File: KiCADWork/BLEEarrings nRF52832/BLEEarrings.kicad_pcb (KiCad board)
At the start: 2 copper layers, 25.5 x 37.8 mm, 37 parts, among them J1 Screw_Terminal_01x01, J2 Screw_Terminal_01x02, J4 Conn_01x06_Pin, SW1 TK-6580B-1, U1 AP7343D-33W5-7, U2 nRF52832-QFxx, Y1 Crystal_GND23

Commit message: Small Bits
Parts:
- moved TP11 5.02 mm to (149.4, 73.6)
- moved J1 2.68 mm to (139.5, 72.4)
- moved J2 2.68 mm to (145.5, 72.4)
- moved C11 2.22 mm to (138.6, 50.5), turned to -90 degrees
- moved TP10 2.13 mm to (139.0, 68.1)
- moved C3 1.77 mm to (148.7, 49.9), turned to -90 degrees
- moved C4 1.71 mm to (144.3, 49.6), turned to 90 degrees
- moved C7 1.42 mm to (139.6, 50.5)
- moved TP3 1.26 mm to (139.5, 46.4)
- moved C6 0.75 mm to (140.5, 50.5), turned to -90 degrees
- moved Y1 0.75 mm to (146.5, 49.9)
- moved C5 0.69 mm to (147.8, 56.5), turned to 90 degrees
- moved L1 0.48 mm to (148.8, 56.5)
- moved TP4 0.42 mm to (149.3, 69.0)
- moved R9 0.33 mm to (149.4, 71.3)
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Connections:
- U1 pad 1: (no net) -> Net-(U1-EN)
- U1 pad 4: (no net) -> unconnected-(U1-NC-Pad4)
- U2 pad 42: unconnected-(U2-P0.30/AIN6-Pad42) -> Net-(U2-P0.30/AIN6)
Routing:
- net +3V3: track 5.12 -> 58.1 mm, vias 0 -> 2
- net NEO_LED: track 0.00 -> 20.3 mm, vias 0 -> 2
- net GND: track 26.3 -> 41.1 mm, vias 0 -> 24
- net +BATT: track 35.7 -> 48.8 mm
- net Net-(J2-Pin_1): track 0.00 -> 11.1 mm
- net Docked: track 0.00 -> 11.1 mm, vias 0 -> 2
- net Net-(U1-EN): track 0.00 -> 10.9 mm
- net LED_A: track 0.00 -> 8.96 mm, vias 0 -> 1
- net Net-(U2-DEC1): track 0.00 -> 2.25 mm
- net Net-(J4-Pin_2): track 9.24 -> 10.7 mm
- net Net-(U2-P0.30/AIN6): track 0.00 -> 0.98 mm, vias 0 -> 1
- net Net-(U2-XC2): track 4.60 -> 5.45 mm
- net Net-(U2-DEC4): track 2.15 -> 1.38 mm
- net Net-(U2-XC1): track 7.47 -> 8.00 mm
- net SWDIO: track 8.00 -> 8.50 mm
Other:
- board size 25.5 x 37.8 mm -> 25.5 x 35.8 mm

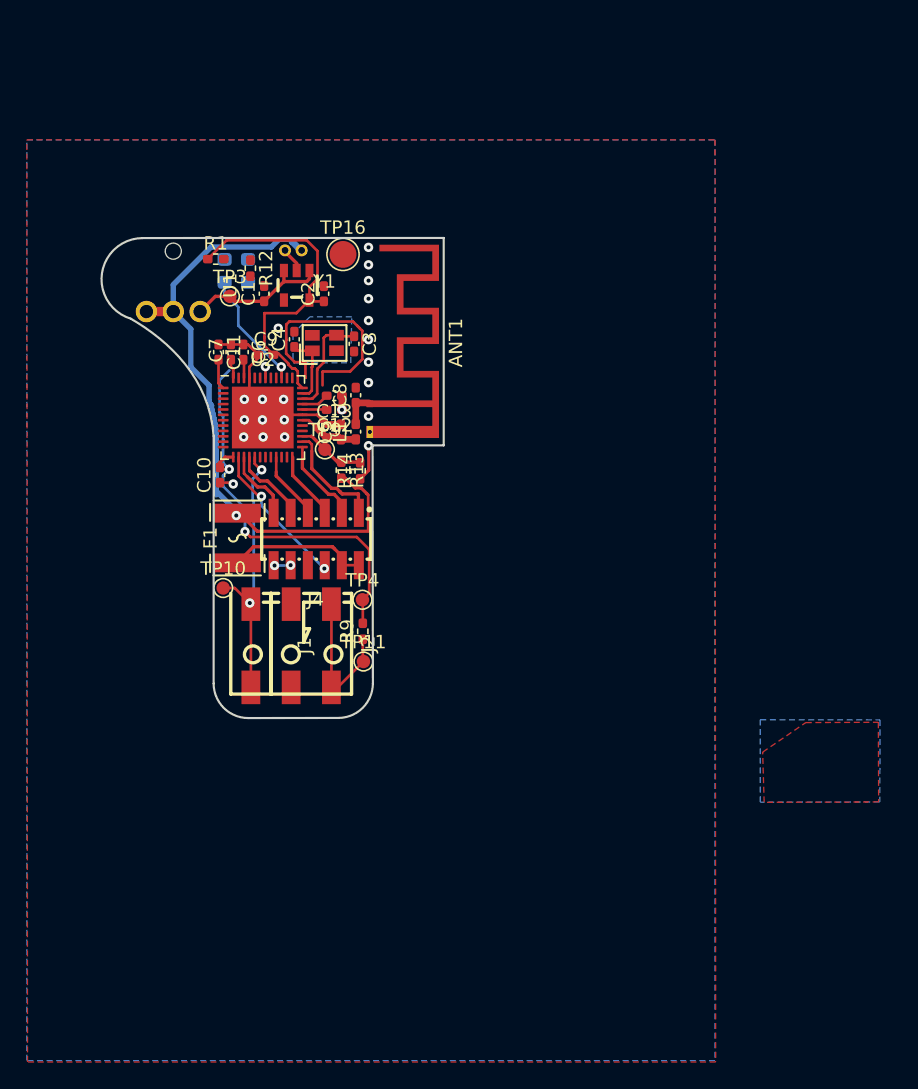
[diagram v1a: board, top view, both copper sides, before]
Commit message: New Chip NRF52833
large changes
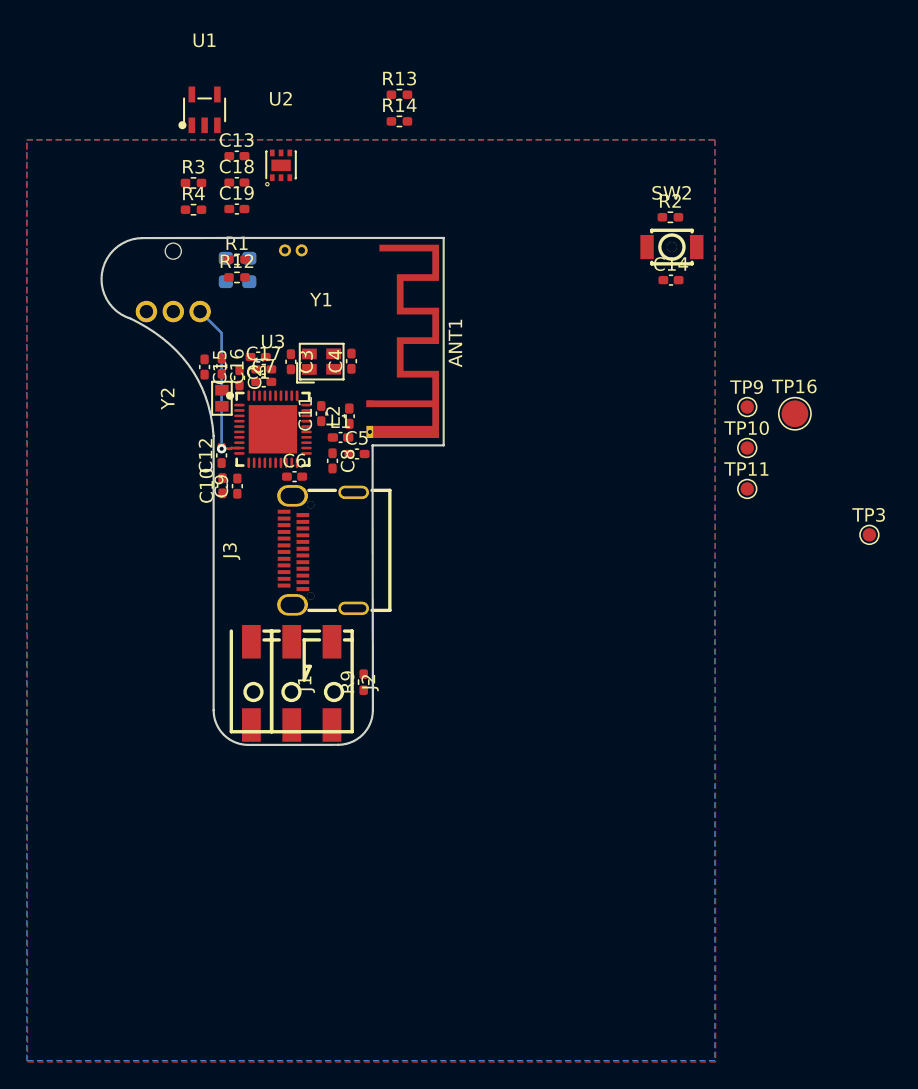
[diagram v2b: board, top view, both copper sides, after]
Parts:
- removed F1: BSMD1812-030-30V, easyeda2kicad:F1812
- removed J4: Conn_01x06_Pin, easyeda2kicad:HDR-SMD_PM127VS-12-12-H34-4.5-R
- removed TP4: TestPoint, TestPoint:TestPoint_Pad_D1.0mm
- added C14: 100n, Capacitor_SMD:C_0402_1005Metric_Pad0.74x0.62mm_HandSolder, F.Cu at (172.3, 45.2)
- added C15: 8p, Capacitor_SMD:C_0402_1005Metric_Pad0.74x0.62mm_HandSolder, F.Cu at (137.6, 51.7)
- added C16: 8p, Capacitor_SMD:C_0402_1005Metric_Pad0.74x0.62mm_HandSolder, F.Cu at (138.9, 51.6)
- added C17: NC, Capacitor_SMD:C_0402_1005Metric_Pad0.74x0.62mm_HandSolder, F.Cu at (142.0, 51.8)
- added C18: 100n, Capacitor_SMD:C_0402_1005Metric_Pad0.74x0.62mm_HandSolder, F.Cu at (140.0, 37.9)
- added C19: 10u, Capacitor_SMD:C_0402_1005Metric_Pad0.74x0.62mm_HandSolder, F.Cu at (140.0, 39.9)
- added J3: USB_C_Receptacle, easyeda2kicad:TYPE-C-SMD_C9900025773, F.Cu at (146.1, 65.3)
- added L2: 2.2n, Inductor_SMD:L_0402_1005Metric_Pad0.77x0.64mm_HandSolder, F.Cu at (148.4, 55.3)
- added R2: 2k, Resistor_SMD:R_0402_1005Metric_Pad0.72x0.64mm_HandSolder, F.Cu at (172.3, 40.5)
- added R3: 100, Resistor_SMD:R_0402_1005Metric_Pad0.72x0.64mm_HandSolder, F.Cu at (136.8, 38.0)
- added R4: 5k6, Resistor_SMD:R_0402_1005Metric_Pad0.72x0.64mm_HandSolder, F.Cu at (136.8, 39.9)
- added SW2: SW_DIP_x01, easyeda2kicad:KEY-SMD_L3.0-W2.5-LS4.0, F.Cu at (172.4, 42.7)
- added U3: NRF52833-QDAA-R7, easyeda2kicad:QFN-40_L5.0-W5.0-P0.40-TL-EP3.6, F.Cu at (142.7, 56.3)
- added Y2: Crystal, easyeda2kicad:CRYSTAL-SMD_L1.6-W1.0, F.Cu at (138.9, 54.0)
- C10, C9: value 100n -> 4.7u
- C11: value 100n -> 100p
- C12: value NC -> 4.7u
- C13: value 100p -> 10u
- C2, C6: value 1u -> 100n
- C3, C4: value 16p -> 12p
- C5: value 0.8p -> 1.2p
- C7: value 4.7u -> 1u
- C8: value 0.8p -> 1p
- D1: value RED LED -> WHITE LED
- L1: value 3.9n -> 4.7n
- R12: value 2k -> 220
- R13: value 5k1 -> 100k
- R14: value 5k1 -> 33k
- U1: value AP7343D-33W5-7 -> MCP73831T-2ACI/OT; footprint easyeda2kicad:SOT-23-5_L2.9-W1.6-P0.95-LS2.8-BR -> easyeda2kicad:SOT-23-5_L3.0-W1.7-P0.95-LS2.8-BL
- U2: value nRF52832-QFxx -> XB6096I2SV; footprint Package_DFN_QFN:QFN-48-1EP_6x6mm_P0.4mm_EP4.6x4.6mm -> easyeda2kicad:WDFN-6_L2.0-W2.0-P0.65-BL-EP
- moved TP3 50.8 mm to (187.1, 64.2)
- moved TP10 40.4 mm to (178.0, 57.7)
- moved TP16 35.7 mm to (181.6, 55.1)
- moved TP9 31.6 mm to (178.0, 54.6)
- moved TP11 31.3 mm to (178.0, 60.7)
- moved R13 28.3 mm to (152.1, 31.4), turned to 0 degrees
- moved R14 26.2 mm to (152.1, 33.4), turned to 0 degrees
- moved C13 19.3 mm to (140.0, 36.0), turned to 0 degrees
- moved U2 18.8 mm to (143.3, 36.6)
- moved U1 14.8 mm to (137.6, 32.5), turned to 0 degrees
- moved C6 10.0 mm to (144.3, 59.8), turned to 0 degrees
- moved C9 10.0 mm to (140.0, 60.5), turned to 90 degrees
- moved C12 9.05 mm to (138.9, 58.2), turned to 90 degrees
- moved C11 8.92 mm to (146.3, 55.1), turned to 90 degrees
- moved C2 8.87 mm to (140.2, 52.5), turned to -90 degrees
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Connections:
- BT1 pad 1: +BATT -> /Power/VBAT
- BT1 pad 2: GND -> Net-(BT1--)
- C1 pad 1: Net-(U1-EN) -> GND
- C1 pad 2: GND -> +3V3
- C10 pad 2: +3V3 -> /DSP/VBUS
- C11 pad 1: GND -> Net-(U3-DEC3)
- C11 pad 2: Net-(U2-DEC1) -> GND
- C12 pad 2: Net-(U2-DEC2) -> +BATT
- C13 pad 1: GND -> /Power/VBAT
- C13 pad 2: Net-(U2-DEC3) -> GND
- C2 pad 1: +3V3 -> GND
- C2 pad 2: GND -> Net-(U3-DEC1)
- C3 pad 1: Net-(U2-XC1) -> GND
- C3 pad 2: GND -> Net-(U3-XC1)
- C4 pad 1: Net-(U2-XC2) -> GND
- C4 pad 2: GND -> Net-(U3-XC1)
- C5 pad 1: Net-(U2-ANT) -> Net-(C5-Pad1)
- C6 pad 1: GND -> +3V3
- C6 pad 2: Net-(U2-DEC4) -> GND
- C7 pad 1: +3V3 -> DEC6
- C8 pad 1: Net-(ANT1-FP) -> Net-(U3-ANT)
- C9 pad 2: +3V3 -> Net-(U3-DECUSB)
- D1 pad 1: GND -> Net-(D1-K)
- D1 pad 2: Net-(D1-A) -> /DSP/VBUS
- L1 pad 1: Net-(U2-ANT) -> Net-(U3-ANT)
- L1 pad 2: Net-(ANT1-FP) -> Net-(C5-Pad1)
- R1 pad 1: +3V3 -> Net-(D1-K)
- R1 pad 2: Net-(D1-A) -> Net-(U1-STAT)
- SW1 pad 1: +BATT -> /Power/VBAT
- SW1 pad 2: +BATT -> /Power/VBAT
- SW1 pad 3: Net-(U1-EN) -> +BATT
- TP3 pad 1: Net-(U1-EN) -> +BATT
- U1 pad 1: Net-(U1-EN) -> Net-(U1-STAT)
- U1 pad 3: Net-(U1-EN) -> /Power/VBAT
- U1 pad 4: unconnected-(U1-NC-Pad4) -> /DSP/VBUS
- U1 pad 5: +3V3 -> Net-(U1-PROG)
- U2 pad 1: Net-(U2-DEC1) -> Net-(U2-VDD)
- U2 pad 2: unconnected-(U2-P0.00/XL1-Pad2) -> GND
- U2 pad 3: unconnected-(U2-P0.01/XL2-Pad3) -> GND
- U2 pad 4: unconnected-(U2-P0.02/AIN0-Pad4) -> Net-(BT1--)
- U2 pad 5: unconnected-(U2-P0.03/AIN1-Pad5) -> Net-(BT1--)
- U2 pad 6: unconnected-(U2-P0.04/AIN2-Pad6) -> Net-(BT1--)
- U2 pad 7: unconnected-(U2-P0.05/AIN3-Pad7) -> GND
- Y1 pad 1: Net-(U2-XC2) -> Net-(U3-XC1)
- Y1 pad 4: Net-(U2-XC1) -> Net-(U3-XC1)
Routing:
- net +3V3: track 58.1 -> 0.00 mm, vias 2 -> 0
- net GND: track 41.1 -> 0.00 mm, vias 24 -> 0
- net +BATT: track 48.8 -> 12.6 mm
- net NEO_LED: track 20.3 -> 0.00 mm, vias 2 -> 0
- net Net-(J2-Pin_1): track 11.1 -> 0.00 mm
- net Docked: track 11.1 -> 0.00 mm, vias 2 -> 0
- net Net-(U1-EN): track 10.9 -> 0.00 mm
- net Net-(J4-Pin_2): track 10.7 -> 0.00 mm
- net LED_A: track 8.96 -> 0.00 mm, vias 1 -> 0
- net SWDIO: track 8.50 -> 0.00 mm
- net Net-(U2-XC1): track 8.00 -> 0.00 mm
- net SWDCLK: track 6.59 -> 0.00 mm
- net Rx: track 6.00 -> 0.00 mm
- net Tx: track 5.62 -> 0.00 mm
- net Net-(U2-XC2): track 5.45 -> 0.00 mm
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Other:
- board size 25.5 x 35.8 mm -> 25.5 x 37.8 mm

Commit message: Dock Updates
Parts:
- added D2: USBLC6-2SC6_C2687116, easyeda2kicad:SOT-23-6_L2.9-W1.6-P0.95-LS2.8-BL, F.Cu at (161.9, 55.0)
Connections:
- J3 pad A6: D+ -> Net-(D2-I/O2-Pad3)
- J3 pad A7: D- -> Net-(D2-I/O1-Pad1)
- J3 pad B6: D+ -> Net-(D2-I/O2-Pad3)
- J3 pad B7: D- -> Net-(D2-I/O1-Pad1)
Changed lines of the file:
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@@
   (net 50 "unconnected-(U3-P0.17-Pad15)")
   (net 51 "unconnected-(U3-P0.15-Pad14)")
+  (net 52 "Net-(D2-I{slash}O1-Pad1)")
+  (net 53 "Net-(D2-I{slash}O2-Pad3)")
   (footprint "easyeda2kicad:WDFN-6_L2.0-W2.0-P0.65-BL-EP" (layer "F.Cu")
     (at 143.285 36.64)
@@
       (net 29 "unconnected-(J3-CC1-PadA5)") (pinfunction "CC1") (pintype "bidirectional+no_connect"))
     (pad "A6" smd rect (at -0.12 -2.59 90) (size 0.3 0.95) (layers "F.Cu" "F.Paste" "F.Mask")
-      (net 30 "D+") (pinfunction "D+") (pintype "bidirectional"))
+      (net 53 "Net-(D2-I{slash}O2-Pad3)") (pinfunction "D+") (pintype "bidirectional"))
     (pad "A7" smd rect (at 0.37 -2.59 90) (size 0.3 0.95) (layers "F.Cu" "F.Paste" "F.Mask")
-      (net 31 "D-") (pinfunction "D-") (pintype "bidirectional"))
+      (net 52 "Net-(D2-I{slash}O1-Pad1)") (pinfunction "D-") (pintype "bidirectional"))
     (pad "A8" smd rect (at 0.88 -2.59 90) (size 0.3 0.95) (layers "F.Cu" "F.Paste" "F.Mask")
       (net 32 "unconnected-(J3-SBU1-PadA8)") (pinfunction "SBU1") (pintype "bidirectional+no_connect"))
@@
       (net 33 "unconnected-(J3-CC2-PadB5)") (pinfunction "CC2") (pintype "bidirectional+no_connect"))
     (pad "B6" smd rect (at 0.12 -1.19 90) (size 0.3 0.95) (layers "F.Cu" "F.Paste" "F.Mask")
-      (net 30 "D+") (pinfunction "D+") (pintype "bidirectional"))
+      (net 53 "Net-(D2-I{slash}O2-Pad3)") (pinfunction "D+") (pintype "bidirectional"))
     (pad "B7" smd rect (at -0.38 -1.19 90) (size 0.3 0.95) (layers "F.Cu" "F.Paste" "F.Mask")
-      (net 31 "D-") (pinfunction "D-") (pintype "bidirectional"))
+      (net 52 "Net-(D2-I{slash}O1-Pad1)") (pinfunction "D-") (pintype "bidirectional"))
     (pad "B8" smd rect (at -0.88 -1.19 90) (size 0.3 0.95) (layers "F.Cu" "F.Paste" "F.Mask")
       (net 34 "unconnected-(J3-SBU2-PadB8)") (pinfunction "SBU2") (pintype "bidirectional+no_connect"))
@@
     )
   )
+  (footprint "easyeda2kicad:SOT-23-6_L2.9-W1.6-P0.95-LS2.8-BL" (layer "F.Cu")
+    (at 161.93 55.04)
+    (property "LCSC Part" "C2687116")
+    (property "Sheetfile" "BLEEarrings.kicad_sch")
+    (property "Sheetname" "")
+    (attr smd)
+    (fp_text reference "D2" (at 0 -5.15) (layer "F.SilkS")
+        (effects (font (size 1 1) (thickness 0.15)))
+    )
+    (fp_text value "USBLC6-2SC6_C2687116" (at 0 5.15) (layer "F.Fab")
+        (effects (font (size 1 1) (thickness 0.15)))
+    )
+    (fp_text user "${REFERENCE}" (at 0 0) (layer "F.Fab")
+        (effects (font (size 1 1) (thickness 0.15)))
+    )
+    (fp_line (start -1.54 0.89) (end -1.54 -0.89)
+      (stroke (width 0.15) (type solid)) (layer "F.SilkS"))
+    (fp_line (start 1.54 0.89) (end 1.54 -0.89)
+      (stroke (width 0.15) (type solid)) (layer "F.SilkS"))
+    (fp_circle (center -1.67 1.3) (end -1.52 1.3)
+      (stroke (width 0.3) (type solid)) (fill none) (layer "F.SilkS"))
+    (fp_circle (center -0.92 1.68) (end -0.82 1.68)
+      (stroke (width 0.2) (type solid)) (fill none) (layer "Cmts.User"))
+    (fp_circle (center -1.46 1.4) (end -1.43 1.4)
+      (stroke (width 0.06) (type solid)) (fill none) (layer "F.Fab"))
+    (pad "1" smd rect (at -0.95 1.15) (size 0.53 1.07) (layers "F.Cu" "F.Paste" "F.Mask")
+      (net 52 "Net-(D2-I{slash}O1-Pad1)") (pinfunction "I/O1") (pintype "unspecified"))
+    (pad "2" smd rect (at 0 1.15) (size 0.53 1.07) (layers "F.Cu" "F.Paste" "F.Mask")
+      (net 1 "GND") (pinfunction "GND") (pintype "unspecified"))
+    (pad "3" smd rect (at 0.95 1.15) (size 0.53 1.07) (layers "F.Cu" "F.Paste" "F.Mask")
+      (net 53 "Net-(D2-I{slash}O2-Pad3)") (pinfunction "I/O2") (pintype "unspecified"))
+    (pad "4" smd rect (at 0.95 -1.15) (size 0.53 1.07) (layers "F.Cu" "F.Paste" "F.Mask")
+      (net 30 "D+") (pinfunction "I/O2") (pintype "unspecified"))
+    (pad "5" smd rect (at 0 -1.15) (size 0.53 1.07) (layers "F.Cu" "F.Paste" "F.Mask")
+      (net 22 "/DSP/VBUS") (pinfunction "VBUS") (pintype "unspecified"))
+    (pad "6" smd rect (at -0.95 -1.15) (size 0.53 1.07) (layers "F.Cu" "F.Paste" "F.Mask")
+      (net 31 "D-") (pinfunction "I/O1") (pintype "unspecified"))
+    (model "${EASYEDA2KICAD}/easyeda2kicad.3dshapes/SOT-23-6_L2.9-W1.6-H1.5-LS2.8-P0.95.wrl"
+      (offset (xyz 0 0 -0))
+      (scale (xyz 1 1 1))
+      (rotate (xyz 0 0 -90))
+    )
+  )

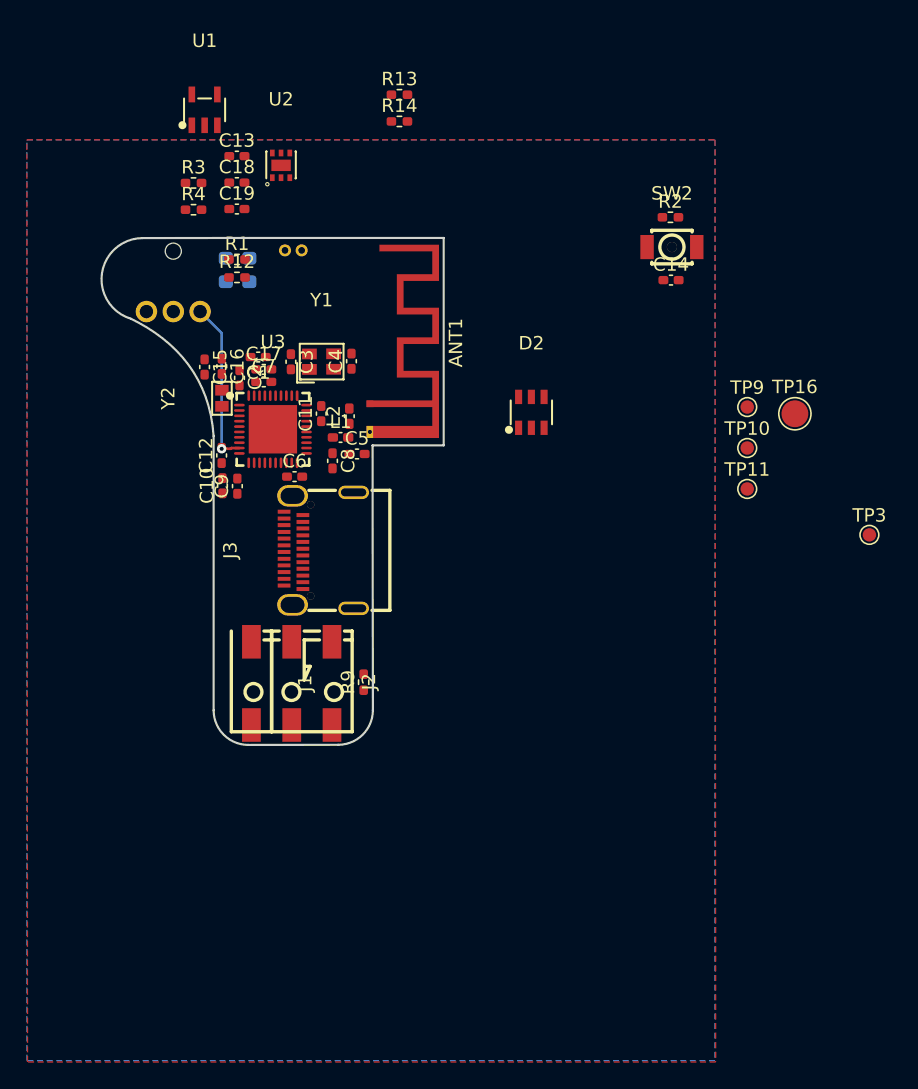
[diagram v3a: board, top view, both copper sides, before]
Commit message: Routing Started on Earrings Again
- Only small routing changes made
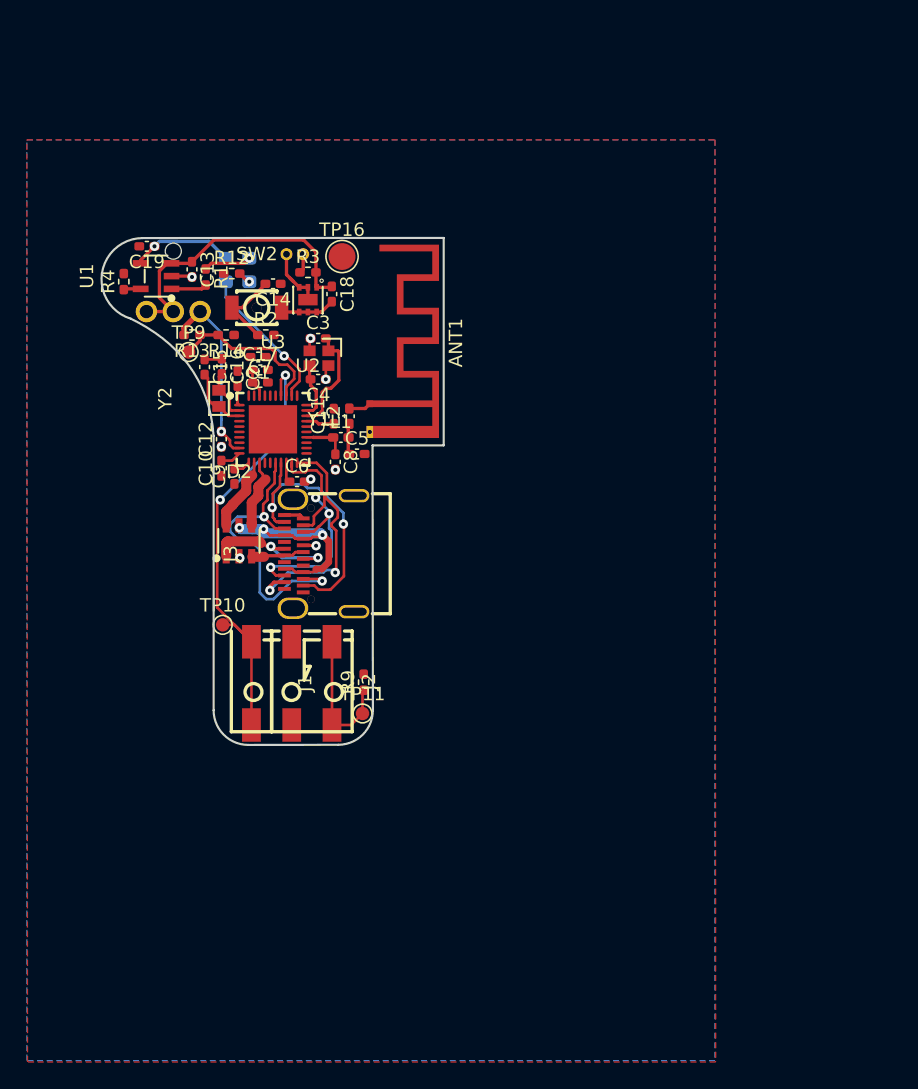
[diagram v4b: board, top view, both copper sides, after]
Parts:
- removed TP3: TestPoint, TestPoint:TestPoint_Pad_D1.0mm
- R4: value 5k6 -> 4k99
- Y1: value Crystal_GND23 -> XL7EL89CKI-111YLC-32M
- Y2: value Crystal -> X161032768KLD2SI
- moved TP9 41.8 mm to (136.4, 50.5)
- moved TP10 41.2 mm to (138.9, 70.9)
- moved TP16 35.7 mm to (147.8, 43.4)
- moved TP11 33.2 mm to (149.4, 77.5)
- moved R2 31.4 mm to (142.2, 49.3)
- moved SW2 31.2 mm to (141.5, 47.2)
- moved C14 29.6 mm to (142.7, 45.5), turned to 180 degrees
- moved D2 23.8 mm to (140.2, 64.6)
- moved R13 23.6 mm to (136.7, 49.3), turned to 180 degrees
- moved R14 20.5 mm to (139.2, 49.3), turned to 180 degrees
- moved U1 12.9 mm to (134.0, 44.9), turned to 90 degrees
- moved C18 10.9 mm to (147.1, 46.2), turned to -90 degrees
- moved R3 10.8 mm to (145.3, 44.6)
- moved U2 10.2 mm to (145.3, 46.6), turned to 180 degrees
- moved C13 9.07 mm to (136.7, 44.4), turned to -90 degrees
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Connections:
- BT1 pad 1: /Power/VBAT -> Net-(BT1-+)
- C18 pad 1: Net-(U2-VDD) -> /Power/VBAT
- C4 pad 2: Net-(U3-XC1) -> Net-(U3-XC2)
- J3 pad A5: unconnected-(J3-CC1-PadA5) -> GND
- J3 pad B5: unconnected-(J3-CC2-PadB5) -> GND
- R3 pad 1: Net-(U2-VDD) -> Net-(BT1-+)
- U2 pad 1: Net-(U2-VDD) -> /Power/VBAT
- U2 pad 2: GND -> Net-(BT1--)
- U2 pad 3: GND -> Net-(BT1--)
- U2 pad 4: Net-(BT1--) -> GND
- U2 pad 5: Net-(BT1--) -> GND
- U2 pad 6: Net-(BT1--) -> GND
- U2 pad 7: GND -> Net-(BT1--)
- U3 pad 17: /DSP/Docked -> SWO
- U3 pad 29: Net-(U3-XC1) -> Net-(U3-XC2)
- Y1 pad 4: Net-(U3-XC1) -> Net-(U3-XC2)
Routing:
- net NEO_LED: track 0.00 -> 33.6 mm, vias 0 -> 2
- net /DSP/VBUS: track 0.00 -> 27.0 mm, vias 0 -> 4
- net nRESET: track 0.00 -> 22.5 mm, vias 0 -> 2
- net /Power/VBAT: track 0.00 -> 22.2 mm
- net SWO: track 0.00 -> 22.0 mm, vias 0 -> 2
- net SWDIO: track 0.00 -> 21.1 mm, vias 0 -> 2
- net SWDCLK: track 0.00 -> 19.0 mm, vias 0 -> 3
- net GND: track 0.00 -> 12.9 mm, vias 0 -> 8
- net BatRef: track 0.00 -> 12.2 mm
- net LED_A: track 0.00 -> 11.1 mm, vias 0 -> 1
- net Net-(D2-I/O1-Pad1): track 0.00 -> 10.8 mm, vias 0 -> 2
- net Net-(J2-Pin_1): track 0.00 -> 10.6 mm
- net Net-(U3-XC1): track 0.00 -> 8.23 mm
- net Pair: track 0.00 -> 6.08 mm
- net D+: track 0.00 -> 5.44 mm
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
